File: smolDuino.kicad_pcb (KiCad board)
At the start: 2 copper layers, 68.6 x 53.3 mm, 63 parts, among them J1 Barrel_Jack_Switch, J2 USB_C_Receptacle_USB2.0, J3 2x3 SPI Header, J4 2x5 HV Outputs, J5 I^{2}C Connector, P1 CONN_01X01, P2 CONN_01X01, P3 CONN_01X01, P4 CONN_01X01, P5 Digital, P6 Power, P7 Digital, P8 Analog, Q1 AO3401A, SW1 Enable, SW2 Reset, U1 AP62250smol_A, U2 rp2040smol-c-unit, U3 74AHCT1G04, U4 Charj_smol, U5 AT24CS02-STUM, U6 SN74AHCT125N

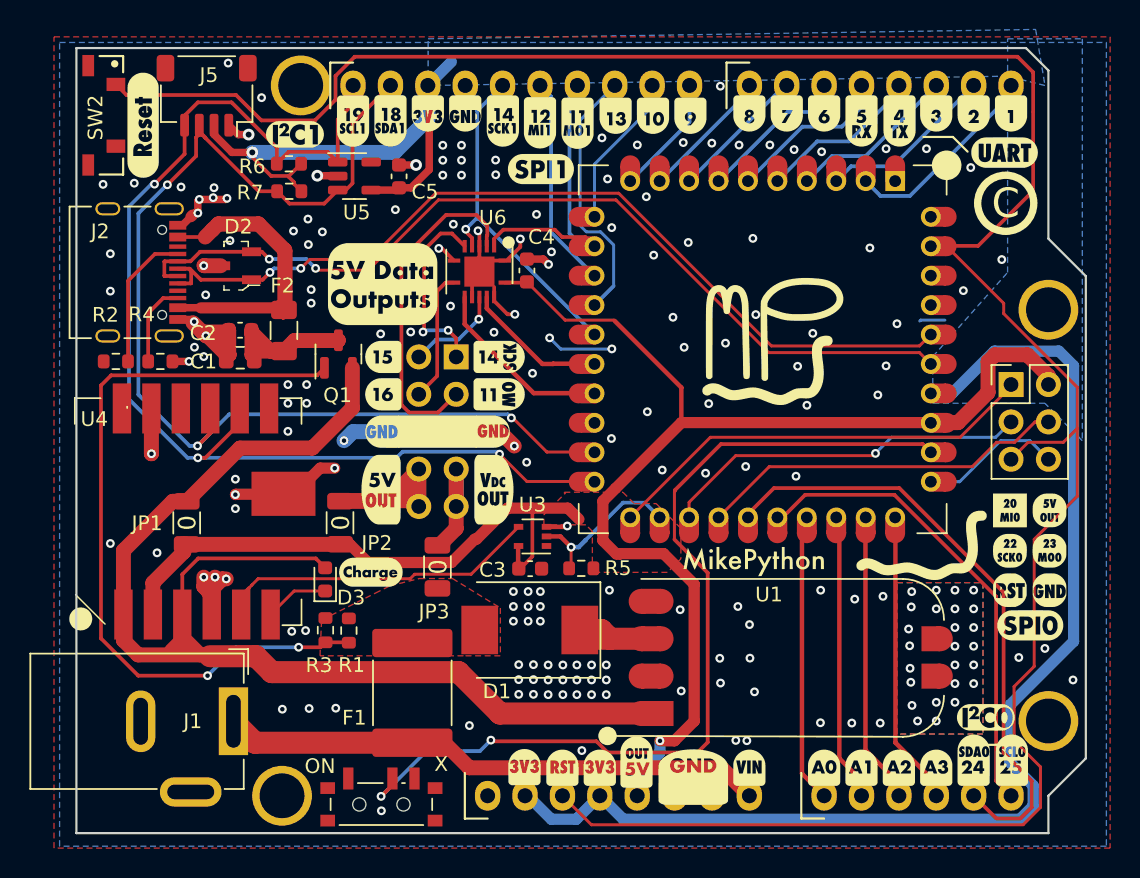
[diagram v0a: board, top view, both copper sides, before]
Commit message: Removed Charjsmol and integrated the charge circuit directly onto the board. Other than the BGA gas gauge IC (which could be deleted without a huge loss) there's no real reason to put the charger on a smol board.
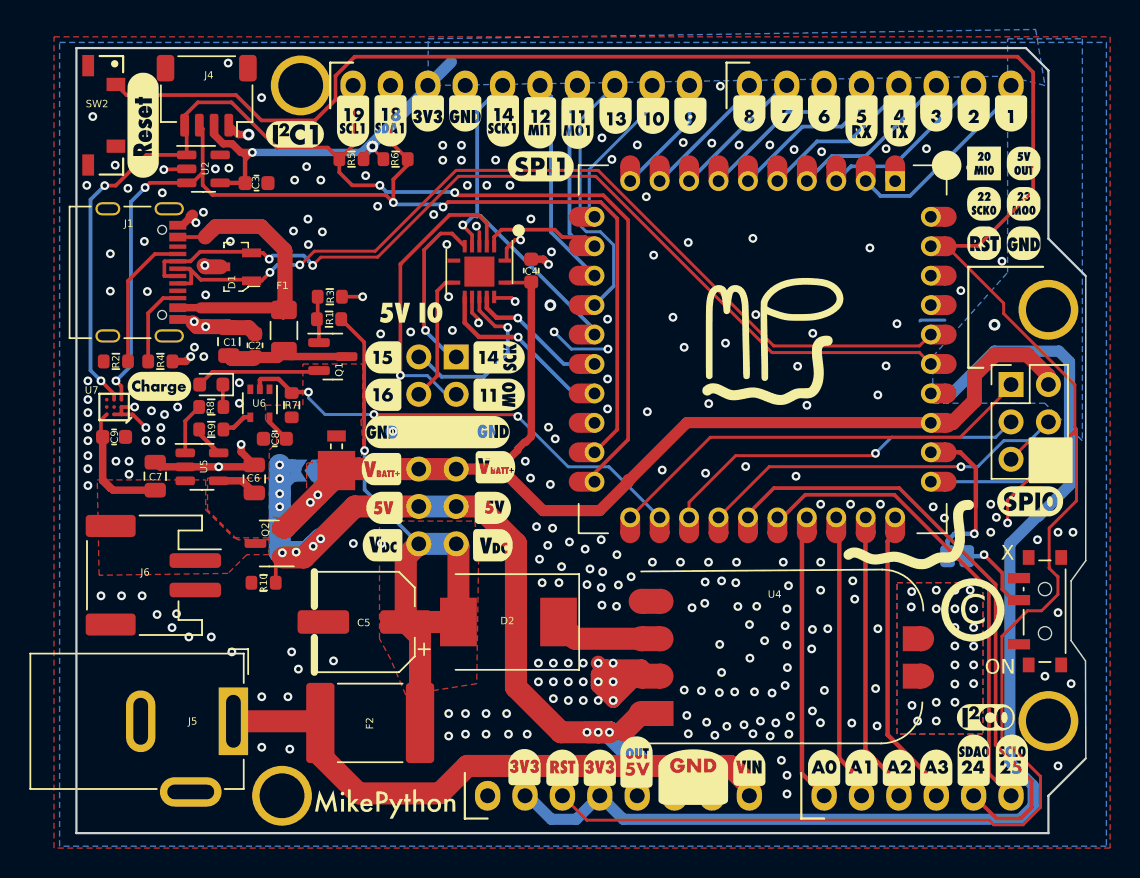
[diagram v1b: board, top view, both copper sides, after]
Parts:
- removed the ART2 at (131.8, 89.1)
- removed the ART4 at (131.5, 88.6)
- removed the G*** at (116.6, 77.7)
- removed the G*** at (174.0, 80.2)
- removed the JP2 at (128.9, 105.3)
- removed JP3: 0, MikeFootprintLib:R_0OHM_1206_3216Metric
- removed the U4 at (114.2, 111.5)
- added C5: 47u, Capacitor_SMD:CP_Elec_6.3x5.4, F.Cu at (130.6, 112.0)
- added C6: 10uF, Capacitor_SMD:C_0805_2012Metric, F.Cu at (123.1, 102.3)
- added C7: 10uF, Capacitor_SMD:C_0805_2012Metric, F.Cu at (116.4, 102.1)
- added C9: 1uF, Capacitor_SMD:C_0603_1608Metric, F.Cu at (113.6, 99.4)
- added D4: UPS120, MikeFootprintLib:UPS120_D_Powermite_AK, F.Cu at (128.7, 101.0)
- added G***: LOGO, LOGO, B.Cu at (135.5, 91.2)
- added G***: LOGO, LOGO, F.Cu at (134.0, 91.2)
- added J6: Battery Connector, Connector_JST:JST_PH_S2B-PH-SM4-TB_1x02-1MP_P2.00mm_Horizontal, F.Cu at (116.2, 108.8)
- added JP1: Jumper_2_Bridged, Jumper:SolderJumper-2_P1.3mm_Bridged_Pad1.0x1.5mm, B.Cu at (170.8, 107.5)
- added Q2: AO3401A, Package_TO_SOT_SMD:SOT-23, F.Cu at (124.1, 106.7)
- added R10: 100K, Resistor_SMD:R_0603_1608Metric, F.Cu at (123.7, 109.4)
- added R8: 1k, Resistor_SMD:R_0603_1608Metric, F.Cu at (120.2, 97.4)
- added R9: 2k, Resistor_SMD:R_0603_1608Metric, F.Cu at (120.2, 98.9)
- added U5: MCP73831-2-OT, Package_TO_SOT_SMD:SOT-23-5, F.Cu at (119.5, 101.5)
- added U7: LC709203FXE-05MH, MikeFootprintLib:WLCSP9-1.60x1.76mm, F.Cu at (113.6, 97.4)
- C1: value 10uF -> 4u7
- C2, C4: value 100nF -> 100n
- C3: renamed from C5; value 100nF -> 100n
- J3: renamed from J4; footprint MikeConnectorFootprints:smolduino_2x05_header -> MikeConnectorFootprints:PinSocket_2x06_P2.54mm_Vertical
- J5: renamed from J1; value Barrel_Jack_Switch -> DC Barrel Jack
- JP2: renamed from JP1; value 0 -> 0 DNP; footprint MikeFootprintLib:R_0OHM_1206_3216Metric -> Jumper:SolderJumper-2_P1.3mm_Open_TrianglePad1.0x1.5mm; moved to B.Cu
- U4: renamed from U1; value AP62250smol_A -> AP62250smol; footprint MikePCBAs:AP62250smol_A -> MikePCBAs:AP62250smol_C
- moved SW1 46.5 mm to (176.5, 111.3), turned to 90 degrees
- moved G*** 30.0 mm to (132.0, 124.4)
- moved MISC2 27.7 mm to (171.9, 111.2)
- moved ART1 23.6 mm to (174.0, 83.6)
- moved R3 22.7 mm to (128.2, 89.9), turned to 0 degrees
- moved R7 22.6 mm to (125.6, 97.3), turned to 90 degrees
- moved R1 21.2 mm to (128.2, 91.4), turned to 180 degrees
- moved U6 20.6 mm to (123.5, 97.2), turned to -90 degrees
- moved C8 19.5 mm to (124.5, 99.6), turned to 180 degrees
- moved G*** 19.1 mm to (116.6, 96.0)
- moved D3 15.3 mm to (120.2, 95.9), turned to 180 degrees
- moved U2 10.3 mm to (119.6, 81.2)
- moved C3 9.69 mm to (123.2, 82.2), turned to 0 degrees
- moved JP2 9.00 mm to (126.8, 101.7), turned to 180 degrees
- moved G*** 8.42 mm to (175.8, 103.9)
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- renumbered ART3 to ART2, ART5 to ART3, ART6 to ART4, ART7 to ART5, ART8 to ART6, C3 to C8, D2 to D1, D1 to D2, F2 to F1, F1 to F2, J2 to J1, J3 to J2, J5 to J4, R6 to R5, R7 to R6, R5 to R7, U2 to U1, U5 to U2, U6 to U3, U3 to U6
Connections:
- net /DC_{In} renamed /Power Supply/DC_{In}
- net /VIN renamed V_{IN}
- net Net-(C1-Pad2) renamed /V_{Bus}_{(Fused)}
- net Net-(F2-Pad1) renamed /V_{Bus}
- net Net-(J2-PadA5) renamed /CC1
- net Net-(J2-PadB5) renamed /CC2
- C8 pad 1: V_{High} -> +5V
- D2 pad 2: /VIN_{Fused} -> V_{DC}
- F2 pad 2: /VIN_{Fused} -> V_{DC}
- J3 pad 10: V_{high_out} -> +5V
- J3 pad 7: V_{DC_out} -> V_{High}
- J3 pad 8: V_{high_out} -> V_{High}
- J3 pad 9: V_{DC_out} -> +5V
- JP2 pad 1: +5V -> V_{High}
- JP2 pad 2: V_{High} -> +5V
- P6 pad 5: V_{High} -> +5V
- R1 pad 1: /VIN_{Fused} -> V_{DC}
- R7 pad 1: V_{High} -> +5V
- U1 pad 32: /EN -> /EN_Pin
- U6 pad 4: Net-(U3-Pad4) -> /Battery Charging (Optional)/ProgSink
- U6 pad 5: V_{High} -> +5V
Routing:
- net /EN: track 62.6 -> 5.13 mm, vias 2 -> 1
- net Net-(Q1-Pad1): track 51.7 -> 2.92 mm, vias 2 -> 0
- net V_{DC}: track 0.00 -> 41.9 mm, vias 0 -> 1
- net V_{High}: track 121.8 -> 83.1 mm, vias 1 -> 2
- net Net-(U3-Pad4): track 21.1 -> 0.00 mm
- net /ChargeEnable: track 11.0 -> 31.9 mm, vias 1 -> 3
- net V_{high_out}: track 18.2 -> 0.00 mm
- net +BATT: track 0.00 -> 15.4 mm
- net GND: track 89.1 -> 77.2 mm, vias 193 -> 286
- net /EN_Pin: track 0.00 -> 11.1 mm, vias 0 -> 1
- net +5V: track 82.1 -> 73.9 mm, vias 0 -> 11
- net V_{DC_out}: track 8.20 -> 0.00 mm
- net /5V_IO15: track 6.67 -> 12.1 mm
- net V_{IN}: track 35.0 -> 40.2 mm
- net /IO19: track 78.3 -> 83.3 mm, vias 3 -> 4
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- added copper zone on F.Cu, net +5V
- added copper zone on F.Cu, net +BATT
- added copper zone on F.Cu, net V_{DC}
- removed copper zone on F.Cu, net /VIN_{Fused}
- removed copper zone on F.Cu, net V_{High}
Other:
- outline, holes or cut-outs redrawn
- board text added: "By Mike in California December 2021"
